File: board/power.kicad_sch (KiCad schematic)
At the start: 38 parts

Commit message: Complete schematic
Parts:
- removed C12, C18, C22: 100nF, Capacitor_SMD:C_0402_1005Metric, symbol Device:C
- removed C14, C16, C21, C23: 10nF, Capacitor_SMD:C_0402_1005Metric, symbol Device:C
- removed C25: 1nF, Capacitor_SMD:C_0402_1005Metric, symbol Device:C
- added C13: 100nF, Capacitor_SMD:C_0402_1005Metric, symbol Device:C
- added C19: 1nF, Capacitor_SMD:C_0402_1005Metric, symbol Device:C
- C15: value 100nF -> 10nF; LCSC C1525 -> C15195
- FPGA1: value LFE5UM-381 -> LFE5U-25F; symbol FPGA_Lattice:LFE5UM-85F-6BG381x -> FPGA_Lattice:LFE5U-85F-8BG381x; JLC (none) -> CABGA-381; LCSC (none) -> C1550939
- renumbered C13 to C10, C10 to C11, C11 to C12, C17 to C14, C19 to C16, C20 to C17, C26 to C18, C24 to C20
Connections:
- net +1V1: now also C13.1, C19.1; no longer FPGA1.T10 (VCCHTX1_D0CH1), FPGA1.T11 (VCCHTX0_D1CH0), FPGA1.T12 (VCCHRX0_D1CH0), FPGA1.T13 (VCCHRX1_D1CH1), FPGA1.T14 (VCCHTX1_D1CH1), FPGA1.T15 (VCCA1), FPGA1.T6 (VCCA0), FPGA1.T7 (VCCHTX0_D0CH0), FPGA1.T8 (VCCHRX0_D0CH0), FPGA1.T9 (VCCHRX1_D0CH1), FPGA1.U15 (VCCA1), FPGA1.U6 (VCCA0)
- net +2V5: no longer FPGA1.V10 (VCCAUXA0), FPGA1.V11 (VCCAUXA0), FPGA1.V17 (VCCAUXA1), FPGA1.V18 (VCCAUXA1)
- net GND: now also FPGA1.T10 (GND), FPGA1.T11 (GND), FPGA1.T12 (GND), FPGA1.T13 (GND), FPGA1.T14 (GND), FPGA1.T15 (GND), FPGA1.T6 (GND), FPGA1.T7 (GND), FPGA1.T8 (GND), FPGA1.T9 (GND), FPGA1.U15 (GND), FPGA1.U6 (GND), FPGA1.V10 (GND), FPGA1.V11 (GND), FPGA1.V17 (GND), FPGA1.V18 (GND), FPGA1.W20 (GND), FPGA1.Y11 (GND), FPGA1.Y12 (GND), FPGA1.Y14 (GND), FPGA1.Y15 (GND), FPGA1.Y16 (GND), FPGA1.Y17 (GND), FPGA1.Y19 (GND), FPGA1.Y5 (GND), FPGA1.Y6 (GND), FPGA1.Y7 (GND), FPGA1.Y8 (GND), C13.2, C19.2
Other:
- moved on the sheet: C11, C12, C18, C8, C9

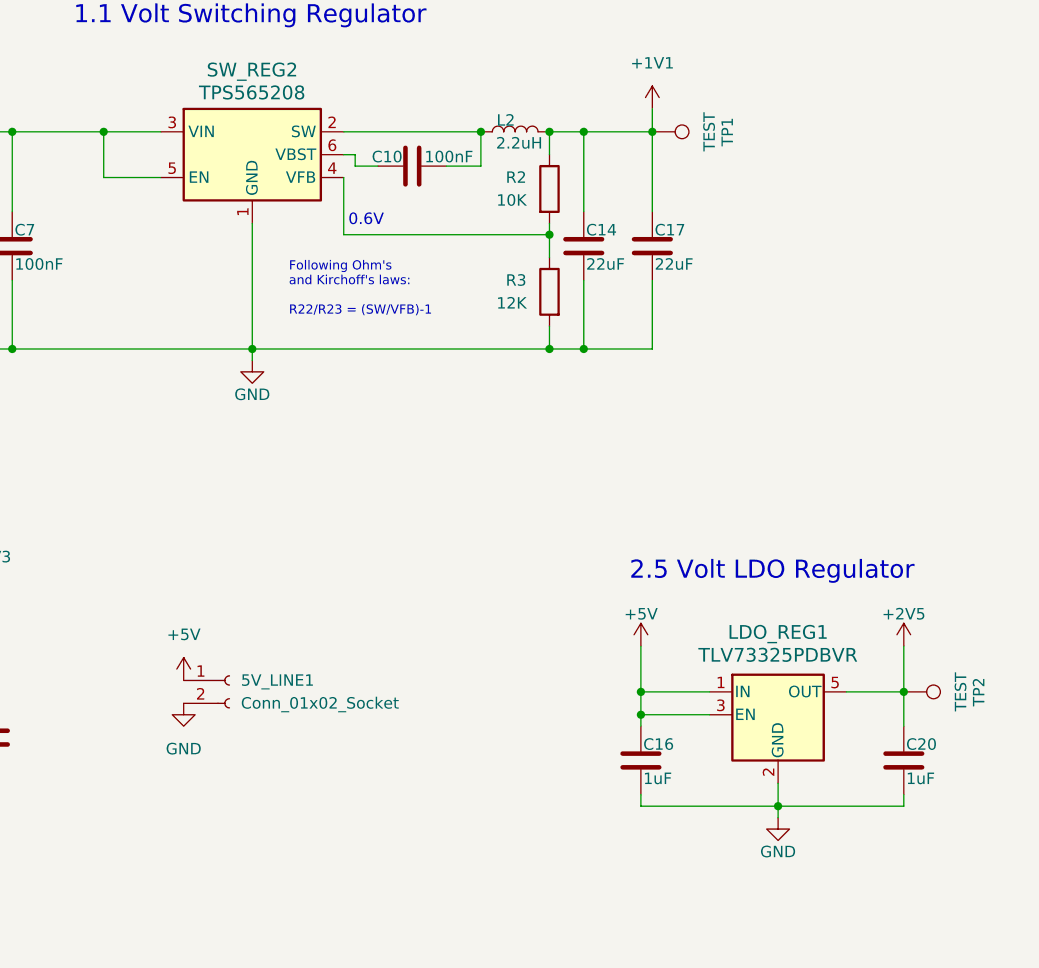
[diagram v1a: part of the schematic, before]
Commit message: Finish routing and remove unneeded silkscreen
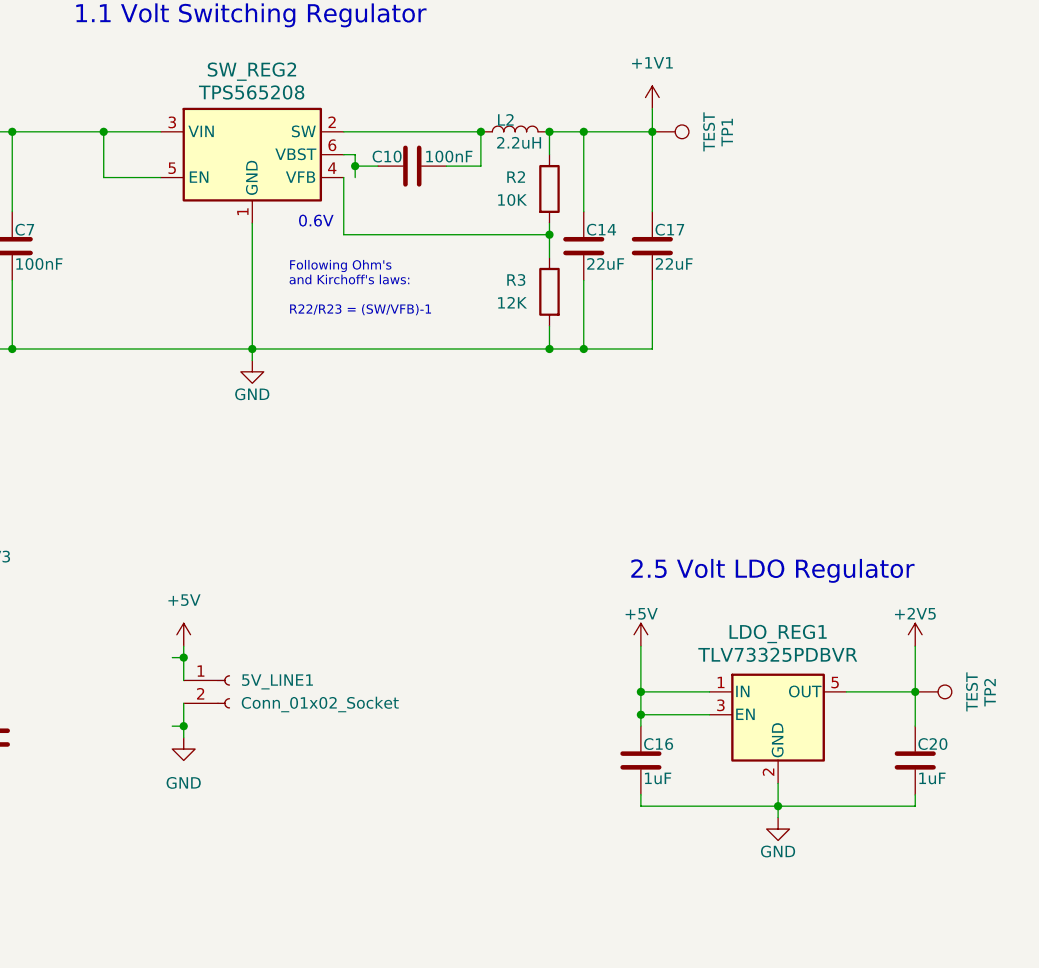
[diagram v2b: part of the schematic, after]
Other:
- moved on the sheet: C20, TP2
